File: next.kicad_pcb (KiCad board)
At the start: 2 copper layers, 351.4 x 99.7 mm, 193 parts, among them J1 USB_mini_micro_B, K0:0 KEYSW, K0:1 KEYSW, K0:2 KEYSW, K0:3 KEYSW, K0:3_1 KEYSW, K0:4 KEYSW, K0:4_1 KEYSW, K10:0 KEYSW, K10:1 KEYSW, K10:2 KEYSW, K10:3 KEYSW, K11:0 KEYSW, K11:1 KEYSW, K11:2 KEYSW, K11:3 KEYSW, K12:0 KEYSW, K12:1 KEYSW, K12:2 KEYSW, K12:3 KEYSW, K13:0 KEYSW, K13:1 KEYSW, K13:2 KEYSW, K13:3 KEYSW, K14:0 KEYSW, K14:1 KEYSW, K14:2 KEYSW, K14:3 KEYSW, K14:4 KEYSW, K14:4_1 KEYSW, K15:0 KEYSW, K15:1 KEYSW, K15:2 KEYSW, K15:3 KEYSW, K15:4 KEYSW, K16:0 KEYSW, K16:1 KEYSW, K16:2 KEYSW, K16:3 KEYSW, K16:4 KEYSW, K1:0 KEYSW, K1:1 KEYSW, K1:2 KEYSW, K1:3 KEYSW, K1:4 KEYSW, K1:4_1 KEYSW, K2:0 KEYSW, K2:1 KEYSW, K2:2 KEYSW, K2:3 KEYSW, K2:4 KEYSW, K2:4_1 KEYSW, K3:0 KEYSW, K3:1 KEYSW, K3:2 KEYSW, K3:3 KEYSW, K3:3_1 KEYSW, K3:4 KEYSW, K4:0 KEYSW, K4:1 KEYSW, K4:2 KEYSW, K4:3 KEYSW, K4:4 KEYSW, K5:0 KEYSW, K5:1 KEYSW, K5:2 KEYSW, K5:3 KEYSW, K5:4 KEYSW, K5:4_1 KEYSW, K6:0 KEYSW, K6:1 KEYSW, K6:2 KEYSW, K6:3 KEYSW, K7:0 KEYSW, K7:1 KEYSW, K7:2 KEYSW, K7:3 KEYSW, K8:0 KEYSW, K8:1 KEYSW, K8:2 KEYSW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

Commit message: V2
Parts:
- removed 7u_Stab: , Keyboard_Footprints:7u_stab
- removed C10: 1uF, Capacitors_SMD:C_0805
- removed the C3 at (200.0, 120.5)
- removed C9: 4.7uF, Capacitors_SMD:C_1206
- removed the D0:4 at (47.6, 104.8)
- removed D10:0, D7:1: D, Keyboard_Footprints:Diode_123
- removed D10:3, D5:4, D7:3, D8:0, D8:1, D8:2, D8:3, D9:0, D9:1, D9:2, D9:3, D9:4: D, Keyboard_Footprints:D_SOD123_axial
- removed K0:4_1, K14:4_1, K16:1, K16:2, K16:3, K16:4, K1:4_1, K2:4_1, K5:4_1: KEYSW, Keyboard_Footprints:Alps_SKCM
- removed the K1:0 at (57.1, 38.1)
- removed the K1:2 at (57.1, 76.2)
- removed the K1:3 at (57.1, 95.2)
- removed the K1:4 at (57.1, 114.3)
- removed LED4: LED, Keyboard_Footprints:LED_Rectangular_W3.9mm_H1.8mm_FlatTop
- removed SJ1, SJ2: SOLDER_JUMPER, Keyboard_Footprints:SOLDER_JUMPER_2
- removed Via (x2): Via, Keyboard_Footprints:Via
- added C8: 0.1uF, Capacitor_SMD:C_0805_2012Metric, B.Cu at (216.5, 107.8)
- added D0:10: D, Diode_SMD:D_SOD-123, B.Cu at (233.4, 40.5)
- added D0:8: D, Keyboard_Footprints:Diode_123_Axial, B.Cu at (181.0, 40.5)
- added D0:9: D, Keyboard_Footprints:Diode_123_Axial, B.Cu at (219.1, 40.5)
- added D1:7: D, Diode_SMD:D_SOD-123, B.Cu at (185.7, 59.5)
- added D1:8: D, Keyboard_Footprints:Diode_123_Axial, B.Cu at (190.5, 59.5)
- added D1:9: D, Keyboard_Footprints:Diode_123_Axial, B.Cu at (228.6, 59.5)
- added D2:8: D, Keyboard_Footprints:Diode_123_Axial, B.Cu at (195.3, 78.6)
- added D2:9: D, Keyboard_Footprints:Diode_123_Axial, B.Cu at (233.4, 78.6)
- added D3:10: D, Diode_SMD:D_SOD-123, B.Cu at (257.2, 97.6)
- added D3:7: D, Diode_SMD:D_SOD-123, B.Cu at (190.5, 97.6)
- added D3:8: D, Keyboard_Footprints:Diode_123_Axial, B.Cu at (204.8, 92.9)
- added D3:9: D, Keyboard_Footprints:Diode_123_Axial, B.Cu at (242.9, 92.9)
- added D4:0: D, Diode_SMD:D_SOD-123, B.Cu at (42.9, 116.7)
- added D4:5: D, Diode_SMD:D_SOD-123, B.Cu at (152.4, 116.7)
- added D4:9: D, Diode_SMD:D_SOD-123, B.Cu at (247.7, 116.7)
- added K0:1: KEYSW, Keyboard_Footprints:Alps, F.Cu at (57.1, 38.1)
- added K1:16: KEYSW, Keyboard_Footprints:Alps, F.Cu at (371.5, 57.1)
- added K2:1: KEYSW, Keyboard_Footprints:Alps, F.Cu at (57.1, 76.2)
- added K2:16: KEYSW, Keyboard_Footprints:Alps, F.Cu at (364.3, 76.2)
- added K3:1: KEYSW, Keyboard_Footprints:Alps, F.Cu at (57.1, 95.2)
- added K3:16: KEYSW, Keyboard_Footprints:Alps, F.Cu at (359.6, 95.2)
- added K4:0_1: KEYSW, Keyboard_Footprints:Alps_Secondary, F.Cu at (47.6, 114.3)
- added K4:1: KEYSW, Keyboard_Footprints:Alps, F.Cu at (57.1, 114.3)
- added K4:16: KEYSW, Keyboard_Footprints:Alps, F.Cu at (366.5, 114.3)
- added K4:1_1: KEYSW, Keyboard_Footprints:Alps_Secondary, F.Cu at (66.7, 114.3)
- added K4:2_1: KEYSW, Keyboard_Footprints:Alps_Secondary, F.Cu at (85.7, 114.3)
- C1, C2, C5, C6, C7: footprint Capacitors_SMD:C_0805 -> Capacitor_SMD:C_0805_2012Metric
- C3: renamed from C8; footprint Capacitors_SMD:C_0805 -> Capacitor_SMD:C_0805_2012Metric
- C4: value 0.1uF -> 4.7uF; footprint Capacitors_SMD:C_0805 -> Capacitor_SMD:C_0805_2012Metric
- D0:0, D1:1, D2:2, D3:3, D4:4: footprint Keyboard_Footprints:Diode_123 -> Diode_SMD:D_SOD-123; moved to B.Cu
- D0:1: renamed from D1:0; footprint Keyboard_Footprints:Diode_123 -> Diode_SMD:D_SOD-123; moved to B.Cu
- D0:11: renamed from D11:0; footprint Keyboard_Footprints:Diode_123 -> Diode_SMD:D_SOD-123; moved to B.Cu
- D0:12: renamed from D12:0; footprint Keyboard_Footprints:Diode_123 -> Diode_SMD:D_SOD-123; moved to B.Cu
- D0:13: renamed from D13:0; footprint Keyboard_Footprints:Diode_123 -> Diode_SMD:D_SOD-123; moved to B.Cu
- D0:14: renamed from D14:0; footprint Keyboard_Footprints:Diode_123 -> Diode_SMD:D_SOD-123; moved to B.Cu
- D0:15: renamed from D15:0; footprint Keyboard_Footprints:Diode_123 -> Diode_SMD:D_SOD-123; moved to B.Cu
- D0:16: renamed from D16:0; footprint Keyboard_Footprints:Diode_123 -> Diode_SMD:D_SOD-123; moved to B.Cu
- D0:2: renamed from D2:0; footprint Keyboard_Footprints:Diode_123 -> Diode_SMD:D_SOD-123; moved to B.Cu
- D0:3: renamed from D3:0; footprint Keyboard_Footprints:Diode_123 -> Diode_SMD:D_SOD-123; moved to B.Cu
- D0:4: renamed from D4:0; footprint Keyboard_Footprints:Diode_123 -> Diode_SMD:D_SOD-123; moved to B.Cu
- D0:5: renamed from D5:0; footprint Keyboard_Footprints:Diode_123 -> Diode_SMD:D_SOD-123; moved to B.Cu
- D0:6: renamed from D6:0; footprint Keyboard_Footprints:Diode_123 -> Diode_SMD:D_SOD-123; moved to B.Cu
- D0:7: renamed from D7:0; footprint Keyboard_Footprints:Diode_123 -> Diode_SMD:D_SOD-123; moved to B.Cu
- D1:0: renamed from D0:1; footprint Keyboard_Footprints:Diode_123 -> Diode_SMD:D_SOD-123; moved to B.Cu
- D1:10: renamed from D10:1; footprint Keyboard_Footprints:Diode_123 -> Diode_SMD:D_SOD-123; moved to B.Cu
- D1:11: renamed from D11:1; footprint Keyboard_Footprints:Diode_123 -> Diode_SMD:D_SOD-123; moved to B.Cu
- D1:12: renamed from D12:1; footprint Keyboard_Footprints:Diode_123 -> Diode_SMD:D_SOD-123; moved to B.Cu
- D1:13: renamed from D13:1; footprint Keyboard_Footprints:Diode_123 -> Diode_SMD:D_SOD-123; moved to B.Cu
- D1:14: renamed from D14:1; footprint Keyboard_Footprints:Diode_123 -> Diode_SMD:D_SOD-123; moved to B.Cu
- D1:15: renamed from D15:1; footprint Keyboard_Footprints:Diode_123 -> Diode_SMD:D_SOD-123; moved to B.Cu
- D1:16: renamed from D16:1; footprint Keyboard_Footprints:Diode_123 -> Diode_SMD:D_SOD-123; moved to B.Cu
- D1:2: renamed from D2:1; footprint Keyboard_Footprints:Diode_123 -> Diode_SMD:D_SOD-123; moved to B.Cu
- D1:3: renamed from D3:1; footprint Keyboard_Footprints:Diode_123 -> Diode_SMD:D_SOD-123; moved to B.Cu
- D1:4: renamed from D4:1; footprint Keyboard_Footprints:Diode_123 -> Diode_SMD:D_SOD-123; moved to B.Cu
- D1:5: renamed from D5:1; footprint Keyboard_Footprints:Diode_123 -> Diode_SMD:D_SOD-123; moved to B.Cu
- D1:6: renamed from D6:1; footprint Keyboard_Footprints:Diode_123 -> Diode_SMD:D_SOD-123; moved to B.Cu
- D2:0: renamed from D0:2; footprint Keyboard_Footprints:Diode_123 -> Diode_SMD:D_SOD-123; moved to B.Cu
- D2:1: renamed from D1:2; footprint Keyboard_Footprints:Diode_123 -> Diode_SMD:D_SOD-123; moved to B.Cu
- D2:10: renamed from D10:2; footprint Keyboard_Footprints:Diode_123 -> Diode_SMD:D_SOD-123; moved to B.Cu
- D2:11: renamed from D11:2; footprint Keyboard_Footprints:Diode_123 -> Diode_SMD:D_SOD-123; moved to B.Cu
- D2:12: renamed from D12:2; footprint Keyboard_Footprints:Diode_123 -> Diode_SMD:D_SOD-123; moved to B.Cu
- D2:13: renamed from D13:2; footprint Keyboard_Footprints:Diode_123 -> Diode_SMD:D_SOD-123; moved to B.Cu
- D2:14: renamed from D14:2; footprint Keyboard_Footprints:Diode_123 -> Diode_SMD:D_SOD-123; moved to B.Cu
- D2:15: renamed from D15:2; footprint Keyboard_Footprints:Diode_123 -> Diode_SMD:D_SOD-123; moved to B.Cu
- D2:16: renamed from D16:2; footprint Keyboard_Footprints:Diode_123 -> Diode_SMD:D_SOD-123; moved to B.Cu
- D2:3: renamed from D3:2; footprint Keyboard_Footprints:Diode_123 -> Diode_SMD:D_SOD-123; moved to B.Cu
- D2:4: renamed from D4:2; footprint Keyboard_Footprints:Diode_123 -> Diode_SMD:D_SOD-123; moved to B.Cu
- D2:5: renamed from D5:2; footprint Keyboard_Footprints:Diode_123 -> Diode_SMD:D_SOD-123; moved to B.Cu
- D2:6: renamed from D6:2; footprint Keyboard_Footprints:Diode_123 -> Diode_SMD:D_SOD-123; moved to B.Cu
- D2:7: renamed from D7:2; footprint Keyboard_Footprints:Diode_123 -> Diode_SMD:D_SOD-123; moved to B.Cu
- D3:0: renamed from D0:3; footprint Keyboard_Footprints:Diode_123 -> Diode_SMD:D_SOD-123; moved to B.Cu
- D3:1: renamed from D1:3; footprint Keyboard_Footprints:Diode_123 -> Diode_SMD:D_SOD-123; moved to B.Cu
- D3:11: renamed from D11:3; footprint Keyboard_Footprints:Diode_123 -> Diode_SMD:D_SOD-123; moved to B.Cu
- D3:12: renamed from D12:3; footprint Keyboard_Footprints:Diode_123 -> Diode_SMD:D_SOD-123; moved to B.Cu
- D3:13: renamed from D13:3; footprint Keyboard_Footprints:Diode_123 -> Diode_SMD:D_SOD-123; moved to B.Cu
- D3:14: renamed from D14:3; footprint Keyboard_Footprints:Diode_123 -> Diode_SMD:D_SOD-123; moved to B.Cu
- D3:15: renamed from D15:3; footprint Keyboard_Footprints:Diode_123 -> Diode_SMD:D_SOD-123; moved to B.Cu
- D3:16: renamed from D16:3; footprint Keyboard_Footprints:Diode_123 -> Diode_SMD:D_SOD-123; moved to B.Cu
- D3:2: renamed from D2:3; footprint Keyboard_Footprints:Diode_123 -> Diode_SMD:D_SOD-123; moved to B.Cu
- D3:4: renamed from D4:3; footprint Keyboard_Footprints:Diode_123 -> Diode_SMD:D_SOD-123; moved to B.Cu
- D3:5: renamed from D5:3; footprint Keyboard_Footprints:Diode_123 -> Diode_SMD:D_SOD-123; moved to B.Cu
- D3:6: renamed from D6:3; footprint Keyboard_Footprints:Diode_123 -> Diode_SMD:D_SOD-123; moved to B.Cu
- D4:1: renamed from D1:4; footprint Keyboard_Footprints:Diode_123 -> Diode_SMD:D_SOD-123; moved to B.Cu
- D4:14: renamed from D14:4; footprint Keyboard_Footprints:Diode_123 -> Diode_SMD:D_SOD-123; moved to B.Cu
- D4:15: renamed from D15:4; footprint Keyboard_Footprints:Diode_123 -> Diode_SMD:D_SOD-123; moved to B.Cu
- D4:16: renamed from D16:4; footprint Keyboard_Footprints:Diode_123 -> Diode_SMD:D_SOD-123; moved to B.Cu
- D4:2: renamed from D2:4; footprint Keyboard_Footprints:Diode_123 -> Diode_SMD:D_SOD-123; moved to B.Cu
- D4:3: renamed from D3:4; footprint Keyboard_Footprints:Diode_123 -> Diode_SMD:D_SOD-123; moved to B.Cu
- K0:0, K1:1, K2:2, K3:3, K4:4: footprint Keyboard_Footprints:Alps_SKCM -> Keyboard_Footprints:Alps
- K0:10: renamed from K10:0; footprint Keyboard_Footprints:Alps_SKCM -> Keyboard_Footprints:Alps
- K0:11: renamed from K11:0; footprint Keyboard_Footprints:Alps_SKCM -> Keyboard_Footprints:Alps
- K0:12: renamed from K12:0; footprint Keyboard_Footprints:Alps_SKCM -> Keyboard_Footprints:Alps
- K0:13: renamed from K13:0; footprint Keyboard_Footprints:Alps_SKCM -> Keyboard_Footprints:Alps
- K0:14: renamed from K14:0; footprint Keyboard_Footprints:Alps_SKCM -> Keyboard_Footprints:Alps
- K0:15: renamed from K15:0; footprint Keyboard_Footprints:Alps_SKCM -> Keyboard_Footprints:Alps
- K0:16: renamed from K16:0; footprint Keyboard_Footprints:Alps_SKCM -> Keyboard_Footprints:Alps
- K0:2: renamed from K2:0; footprint Keyboard_Footprints:Alps_SKCM -> Keyboard_Footprints:Alps
- K0:3: renamed from K3:0; footprint Keyboard_Footprints:Alps_SKCM -> Keyboard_Footprints:Alps
- K0:3_1, K3:3_1: footprint Keyboard_Footprints:Alps_SKCM -> Keyboard_Footprints:Alps_Secondary
- K0:4: renamed from K4:0; footprint Keyboard_Footprints:Alps_SKCM -> Keyboard_Footprints:Alps
- K0:5: renamed from K5:0; footprint Keyboard_Footprints:Alps_SKCM -> Keyboard_Footprints:Alps
- K0:6: renamed from K6:0; footprint Keyboard_Footprints:Alps_SKCM -> Keyboard_Footprints:Alps
- K0:7: renamed from K7:0; footprint Keyboard_Footprints:Alps_SKCM -> Keyboard_Footprints:Alps
- K0:8: renamed from K8:0; footprint Keyboard_Footprints:Alps_SKCM -> Keyboard_Footprints:Alps
- K0:9: renamed from K9:0; footprint Keyboard_Footprints:Alps_SKCM -> Keyboard_Footprints:Alps
- K1:0: renamed from K0:1; footprint Keyboard_Footprints:Alps_SKCM -> Keyboard_Footprints:Alps
- K1:10: renamed from K10:1; footprint Keyboard_Footprints:Alps_SKCM -> Keyboard_Footprints:Alps
- K1:11: renamed from K11:1; footprint Keyboard_Footprints:Alps_SKCM -> Keyboard_Footprints:Alps
- K1:12: renamed from K12:1; footprint Keyboard_Footprints:Alps_SKCM -> Keyboard_Footprints:Alps
- K1:13: renamed from K13:1; footprint Keyboard_Footprints:Alps_SKCM -> Keyboard_Footprints:Alps
- K1:14: renamed from K14:1; footprint Keyboard_Footprints:Alps_SKCM -> Keyboard_Footprints:Alps
- K1:15: renamed from K15:1; footprint Keyboard_Footprints:Alps_SKCM -> Keyboard_Footprints:Alps
- K1:2: renamed from K2:1; footprint Keyboard_Footprints:Alps_SKCM -> Keyboard_Footprints:Alps
- K1:3: renamed from K3:1; footprint Keyboard_Footprints:Alps_SKCM -> Keyboard_Footprints:Alps
- K1:4: renamed from K4:1; footprint Keyboard_Footprints:Alps_SKCM -> Keyboard_Footprints:Alps
- K1:5: renamed from K5:1; footprint Keyboard_Footprints:Alps_SKCM -> Keyboard_Footprints:Alps
- K1:6: renamed from K6:1; footprint Keyboard_Footprints:Alps_SKCM -> Keyboard_Footprints:Alps
- K1:7: renamed from K7:1; footprint Keyboard_Footprints:Alps_SKCM -> Keyboard_Footprints:Alps
- K1:8: renamed from K8:1; footprint Keyboard_Footprints:Alps_SKCM -> Keyboard_Footprints:Alps
- K1:9: renamed from K9:1; footprint Keyboard_Footprints:Alps_SKCM -> Keyboard_Footprints:Alps
- K2:0: renamed from K0:2; footprint Keyboard_Footprints:Alps_SKCM -> Keyboard_Footprints:Alps
- K2:10: renamed from K10:2; footprint Keyboard_Footprints:Alps_SKCM -> Keyboard_Footprints:Alps
- K2:11: renamed from K11:2; footprint Keyboard_Footprints:Alps_SKCM -> Keyboard_Footprints:Alps
- K2:12: renamed from K12:2; footprint Keyboard_Footprints:Alps_SKCM -> Keyboard_Footprints:Alps
- K2:13: renamed from K13:2; footprint Keyboard_Footprints:Alps_SKCM -> Keyboard_Footprints:Alps
- K2:14: renamed from K14:2; footprint Keyboard_Footprints:Alps_SKCM -> Keyboard_Footprints:Alps
- K2:15: renamed from K15:2; footprint Keyboard_Footprints:Alps_SKCM -> Keyboard_Footprints:Alps
- K2:3: renamed from K3:2; footprint Keyboard_Footprints:Alps_SKCM -> Keyboard_Footprints:Alps
- K2:4: renamed from K4:2; footprint Keyboard_Footprints:Alps_SKCM -> Keyboard_Footprints:Alps
- K2:5: renamed from K5:2; footprint Keyboard_Footprints:Alps_SKCM -> Keyboard_Footprints:Alps
- K2:6: renamed from K6:2; footprint Keyboard_Footprints:Alps_SKCM -> Keyboard_Footprints:Alps
- K2:7: renamed from K7:2; footprint Keyboard_Footprints:Alps_SKCM -> Keyboard_Footprints:Alps
- K2:8: renamed from K8:2; footprint Keyboard_Footprints:Alps_SKCM -> Keyboard_Footprints:Alps
- K2:9: renamed from K9:2; footprint Keyboard_Footprints:Alps_SKCM -> Keyboard_Footprints:Alps
- K3:0: renamed from K0:3; footprint Keyboard_Footprints:Alps_SKCM -> Keyboard_Footprints:Alps
- K3:10: renamed from K10:3; footprint Keyboard_Footprints:Alps_SKCM -> Keyboard_Footprints:Alps
- K3:11: renamed from K11:3; footprint Keyboard_Footprints:Alps_SKCM -> Keyboard_Footprints:Alps
- K3:12: renamed from K12:3; footprint Keyboard_Footprints:Alps_SKCM -> Keyboard_Footprints:Alps
- K3:13: renamed from K13:3; footprint Keyboard_Footprints:Alps_SKCM -> Keyboard_Footprints:Alps
- K3:14: renamed from K14:3; footprint Keyboard_Footprints:Alps_SKCM -> Keyboard_Footprints:Alps
- K3:15: renamed from K15:3; footprint Keyboard_Footprints:Alps_SKCM -> Keyboard_Footprints:Alps
- K3:2: renamed from K2:3; footprint Keyboard_Footprints:Alps_SKCM -> Keyboard_Footprints:Alps
- K3:4: renamed from K4:3; footprint Keyboard_Footprints:Alps_SKCM -> Keyboard_Footprints:Alps
- K3:5: renamed from K5:3; footprint Keyboard_Footprints:Alps_SKCM -> Keyboard_Footprints:Alps
- K3:6: renamed from K6:3; footprint Keyboard_Footprints:Alps_SKCM -> Keyboard_Footprints:Alps
- K3:7: renamed from K7:3; footprint Keyboard_Footprints:Alps_SKCM -> Keyboard_Footprints:Alps
- K3:8: renamed from K8:3; footprint Keyboard_Footprints:Alps_SKCM -> Keyboard_Footprints:Alps
- K3:9: renamed from K9:3; footprint Keyboard_Footprints:Alps_SKCM -> Keyboard_Footprints:Alps
- K4:0: renamed from K0:4; footprint Keyboard_Footprints:Alps_SKCM -> Keyboard_Footprints:Alps
- K4:14: renamed from K14:4; footprint Keyboard_Footprints:Alps_SKCM -> Keyboard_Footprints:Alps
- K4:15: renamed from K15:4; footprint Keyboard_Footprints:Alps_SKCM -> Keyboard_Footprints:Alps
- K4:2: renamed from K2:4; footprint Keyboard_Footprints:Alps_SKCM -> Keyboard_Footprints:Alps
- K4:3: renamed from K3:4; footprint Keyboard_Footprints:Alps_SKCM -> Keyboard_Footprints:Alps
- K4:5: renamed from K5:4; footprint Keyboard_Footprints:Alps_SKCM -> Keyboard_Footprints:Alps
- K4:9: renamed from K9:4; footprint Keyboard_Footprints:Alps_SKCM -> Keyboard_Footprints:Alps
- LED1, LED2, LED3: footprint Keyboard_Footprints:LED_Rectangular_W3.9mm_H1.8mm_FlatTop -> LED_THT:LED_D3.0mm
- R1, R2, R3, R5, R6, R7: footprint Resistors_SMD:R_0805 -> Resistor_SMD:R_0805_2012Metric
- R4: value 1k -> 10k; footprint Resistors_SMD:R_0805 -> Resistor_SMD:R_0805_2012Metric
- SW1: value SW_JUMP -> RESET; footprint Pin_Headers:Pin_Header_Straight_1x02_Pitch1.27mm -> Keyboard_Footprints:TE_1825966-1; moved to B.Cu
- U1: footprint Keyboard_Footprints:ATmega32U4-AU -> Package_QFP:LQFP-44_10x10mm_P0.8mm
- X1: value XTAL_GND -> 16MHz_12pF; footprint Keyboard_Footprints:Crystal_SMD_3225-4pin_3.2x2.5mm -> Crystal:Crystal_SMD_SeikoEpson_FA238-4Pin_3.2x2.5mm
- moved R4 167.8 mm to (348.5, 115.2), turned to -90 degrees
- moved C7 26.5 mm to (193.0, 108.0), turned to 180 degrees
- moved C4 16.1 mm to (221.2, 111.2), turned to 90 degrees
- moved D4:1 12.8 mm to (61.9, 116.7), turned to 90 degrees
- moved C6 12.6 mm to (208.5, 101.0)
- moved D4:3 10.6 mm to (100.0, 116.7), turned to 90 degrees
- moved C5 10.6 mm to (199.2, 120.0), turned to 90 degrees
- moved D0:15 9.53 mm to (328.6, 40.5), turned to 90 degrees
- moved D0:16 9.53 mm to (371.5, 40.5), turned to 90 degrees
- moved D1:12 9.53 mm to (281.0, 59.5), turned to 90 degrees
- moved D1:13 9.53 mm to (300.0, 59.5), turned to 90 degrees
- moved D1:16 9.53 mm to (376.2, 59.5), turned to 90 degrees
- moved D2:13 9.53 mm to (304.8, 78.6), turned to 90 degrees
- moved D2:14 9.53 mm to (323.9, 78.6), turned to 90 degrees
- moved D3:11 9.53 mm to (276.2, 97.6), turned to 90 degrees
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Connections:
- net Net-(D0:0-Pad1) renamed Row0
- net Net-(D0:4-Pad1) renamed Row4
- net Net-(K0:0-Pad1) renamed Col0
- net Net-(K1:0-Pad1) renamed Col1
- net Net-(K2:0-Pad1) renamed Col2
- net Net-(K3:0-Pad1) renamed Col3
- C7 pad 1: Net-(C7-Pad1) -> +5V
- D1:0 pad 1: Net-(D0:1-Pad1) -> Row1
- D1:1 pad 1: Net-(D0:1-Pad1) -> Row1
- D1:10 pad 1: Net-(D0:1-Pad1) -> Row1
- D1:11 pad 1: Net-(D0:1-Pad1) -> Row1
- D1:12 pad 1: Net-(D0:1-Pad1) -> Row1
- D1:13 pad 1: Net-(D0:1-Pad1) -> Row1
- D1:14 pad 1: Net-(D0:1-Pad1) -> Row1
- D1:15 pad 1: Net-(D0:1-Pad1) -> Row1
- D1:16 pad 1: Net-(D0:1-Pad1) -> Row1
- D1:2 pad 1: Net-(D0:1-Pad1) -> Row1
- D1:3 pad 1: Net-(D0:1-Pad1) -> Row1
- D1:4 pad 1: Net-(D0:1-Pad1) -> Row1
- D1:5 pad 1: Net-(D0:1-Pad1) -> Row1
- D1:6 pad 1: Net-(D0:1-Pad1) -> Row1
- D2:0 pad 1: Net-(D0:2-Pad1) -> Row2
- D2:1 pad 1: Net-(D0:2-Pad1) -> Row2
- D2:10 pad 1: Net-(D0:2-Pad1) -> Row2
- D2:11 pad 1: Net-(D0:2-Pad1) -> Row2
- D2:12 pad 1: Net-(D0:2-Pad1) -> Row2
- D2:13 pad 1: Net-(D0:2-Pad1) -> Row2
- D2:14 pad 1: Net-(D0:2-Pad1) -> Row2
- D2:15 pad 1: Net-(D0:2-Pad1) -> Row2
- D2:16 pad 1: Net-(D0:2-Pad1) -> Row2
- D2:2 pad 1: Net-(D0:2-Pad1) -> Row2
- D2:3 pad 1: Net-(D0:2-Pad1) -> Row2
- D2:4 pad 1: Net-(D0:2-Pad1) -> Row2
- D2:5 pad 1: Net-(D0:2-Pad1) -> Row2
- D2:6 pad 1: Net-(D0:2-Pad1) -> Row2
- D2:7 pad 1: Net-(D0:2-Pad1) -> Row2
- D3:0 pad 1: Net-(D0:3-Pad1) -> Row3
- D3:1 pad 1: Net-(D0:3-Pad1) -> Row3
- D3:11 pad 1: Net-(D0:3-Pad1) -> Row3
- D3:12 pad 1: Net-(D0:3-Pad1) -> Row3
- D3:13 pad 1: Net-(D0:3-Pad1) -> Row3
- D3:14 pad 1: Net-(D0:3-Pad1) -> Row3
- D3:15 pad 1: Net-(D0:3-Pad1) -> Row3
- D3:16 pad 1: Net-(D0:3-Pad1) -> Row3
- D3:2 pad 1: Net-(D0:3-Pad1) -> Row3
- D3:3 pad 1: Net-(D0:3-Pad1) -> Row3
- D3:4 pad 1: Net-(D0:3-Pad1) -> Row3
- D3:5 pad 1: Net-(D0:3-Pad1) -> Row3
- D3:6 pad 1: Net-(D0:3-Pad1) -> Row3
- J1 pad 4: Net-(J1-Pad4) -> unconnected-(J1-Pad4)
- J1 pad 6: Net-(J1-Pad6) -> unconnected-(J1-Pad6)
- K0:10 pad 1: Net-(K10:0-Pad1) -> Col10
- K0:11 pad 1: Net-(K11:0-Pad1) -> Col11
- K0:12 pad 1: Net-(K12:0-Pad1) -> Col12
- K0:13 pad 1: Net-(K13:0-Pad1) -> Col13
- K0:14 pad 1: Net-(K14:0-Pad1) -> Col14
- K0:15 pad 1: Net-(K15:0-Pad1) -> Col15
- K0:16 pad 1: Net-(K16:0-Pad1) -> Col16
- K0:4 pad 1: Net-(K4:0-Pad1) -> Col4
- K0:5 pad 1: Net-(K5:0-Pad1) -> Col5
- K0:6 pad 1: Net-(K6:0-Pad1) -> Col6
- K0:7 pad 1: Net-(K7:0-Pad1) -> Col7
- K0:8 pad 1: Net-(K8:0-Pad1) -> Col8
- K0:9 pad 1: Net-(K9:0-Pad1) -> Col9
- K1:10 pad 1: Net-(K10:0-Pad1) -> Col10
- K1:11 pad 1: Net-(K11:0-Pad1) -> Col11
- K1:12 pad 1: Net-(K12:0-Pad1) -> Col12
- K1:13 pad 1: Net-(K13:0-Pad1) -> Col13
- K1:14 pad 1: Net-(K14:0-Pad1) -> Col14
- K1:15 pad 1: Net-(K15:0-Pad1) -> Col15
- K1:4 pad 1: Net-(K4:0-Pad1) -> Col4
- K1:5 pad 1: Net-(K5:0-Pad1) -> Col5
- K1:6 pad 1: Net-(K6:0-Pad1) -> Col6
- K1:7 pad 1: Net-(K7:0-Pad1) -> Col7
- K1:8 pad 1: Net-(K8:0-Pad1) -> Col8
- K1:9 pad 1: Net-(K9:0-Pad1) -> Col9
- K2:10 pad 1: Net-(K10:0-Pad1) -> Col10
- K2:11 pad 1: Net-(K11:0-Pad1) -> Col11
- K2:12 pad 1: Net-(K12:0-Pad1) -> Col12
- K2:13 pad 1: Net-(K13:0-Pad1) -> Col13
- K2:14 pad 1: Net-(K14:0-Pad1) -> Col14
- K2:15 pad 1: Net-(K15:0-Pad1) -> Col15
- K2:4 pad 1: Net-(K4:0-Pad1) -> Col4
- K2:5 pad 1: Net-(K5:0-Pad1) -> Col5
- K2:6 pad 1: Net-(K6:0-Pad1) -> Col6
- K2:7 pad 1: Net-(K7:0-Pad1) -> Col7
- K2:8 pad 1: Net-(K8:0-Pad1) -> Col8
- K2:9 pad 1: Net-(K9:0-Pad1) -> Col9
- K3:10 pad 1: Net-(K10:0-Pad1) -> Col10
- K3:11 pad 1: Net-(K11:0-Pad1) -> Col11
- K3:12 pad 1: Net-(K12:0-Pad1) -> Col12
- K3:13 pad 1: Net-(K13:0-Pad1) -> Col13
- K3:14 pad 1: Net-(K14:0-Pad1) -> Col14
- K3:15 pad 1: Net-(K15:0-Pad1) -> Col15
- K3:4 pad 1: Net-(K4:0-Pad1) -> Col4
- K3:5 pad 1: Net-(K5:0-Pad1) -> Col5
- K3:6 pad 1: Net-(K6:0-Pad1) -> Col6
- K3:7 pad 1: Net-(K7:0-Pad1) -> Col7
- K3:8 pad 1: Net-(K8:0-Pad1) -> Col8
- K3:9 pad 1: Net-(K9:0-Pad1) -> Col9
- K4:14 pad 1: Net-(K14:0-Pad1) -> Col14
- K4:15 pad 1: Net-(K15:0-Pad1) -> Col15
- K4:4 pad 1: Net-(K4:0-Pad1) -> Col4
- K4:5 pad 1: Net-(K5:0-Pad1) -> Col5
- K4:9 pad 1: Net-(K9:0-Pad1) -> Col9
- R4 pad 1: GND -> +5V
- R4 pad 2: Net-(LED4-Pad2) -> Net-(R4-Pad2)
- R5 pad 1: Net-(LED1-Pad2) -> Net-(LED1-Pad1)
- R6 pad 1: Net-(LED2-Pad2) -> Net-(LED2-Pad1)
- R7 pad 1: Net-(LED3-Pad2) -> Net-(LED3-Pad1)
- SW1 pad 2: Net-(SW1-Pad2) -> Net-(R4-Pad2)
- U1 pad 10: Net-(K16:0-Pad1) -> Col14
- U1 pad 11: Net-(D0:2-Pad1) -> Col15
- U1 pad 12: Net-(D0:1-Pad1) -> Net-(LED3-Pad2)
- U1 pad 13: Net-(SW1-Pad2) -> Net-(R4-Pad2)
- U1 pad 22: Net-(LED1-Pad1) -> Col4
- U1 pad 26: Net-(SJ1-Pad1) -> Col5
- U1 pad 27: Net-(LED3-Pad1) -> Col6
- U1 pad 28: Net-(K4:0-Pad1) -> Col16
- U1 pad 29: Net-(K5:0-Pad1) -> Net-(LED1-Pad2)
- U1 pad 30: Net-(K6:0-Pad1) -> Net-(LED2-Pad2)
- U1 pad 31: Net-(K7:0-Pad1) -> Col10
- U1 pad 32: Net-(D0:3-Pad1) -> Col11
- U1 pad 36: Net-(K8:0-Pad1) -> Row3
- U1 pad 37: Net-(K9:0-Pad1) -> Row2
- U1 pad 38: Net-(K10:0-Pad1) -> Row1
- U1 pad 39: Net-(K11:0-Pad1) -> Col9
- U1 pad 40: Net-(K12:0-Pad1) -> Col8
- U1 pad 41: Net-(K13:0-Pad1) -> Col7
- U1 pad 42: Net-(C7-Pad1) -> unconnected-(U1-Pad42)
- U1 pad 8: Net-(K14:0-Pad1) -> Col12
- U1 pad 9: Net-(K15:0-Pad1) -> Col13
- X1 pad 2: Net-(C2-Pad1) -> GND
- X1 pad 3: GND -> Net-(C2-Pad1)
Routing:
- net Net-(D0:1-Pad1): track 558.1 -> 0.00 mm, vias 2 -> 0
- net Net-(D0:2-Pad1): track 513.7 -> 0.00 mm, vias 2 -> 0
- net Net-(D0:3-Pad1): track 410.7 -> 0.00 mm
- net Row3: track 0.00 -> 397.9 mm, vias 0 -> 1
- net Row1: track 0.00 -> 388.5 mm
- net GND: track 128.6 -> 516.4 mm, vias 19 -> 7
- net Row2: track 0.00 -> 362.2 mm
- net Net-(K15:0-Pad1): track 274.5 -> 0.00 mm, vias 1 -> 0
- net Col16: track 0.00 -> 270.6 mm, vias 0 -> 2
- net Net-(K16:0-Pad1): track 262.8 -> 0.00 mm, vias 2 -> 0
- net Col15: track 0.00 -> 261.0 mm, vias 0 -> 1
- net Net-(K14:0-Pad1): track 250.8 -> 0.00 mm
- net Net-(LED3-Pad1): track 247.8 -> 4.30 mm, vias 4 -> 0
- net Col14: track 0.00 -> 230.5 mm, vias 0 -> 1
- net Net-(LED1-Pad2): track 2.54 -> 218.5 mm
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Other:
- net class D2 removed
- net class D3 removed
- net class D4 removed
- net class Default removed
- rule pad_to_mask_clearance: 0.2 -> 0
- board text added: "NeXT76 by Andrew D Rev 1.1"
- board text removed: "NeXT76 by Andrew D Rev 1.0"

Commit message: Update Model
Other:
- board text added: "NeXT76 by Andrew D Rev 1.0"
- board text removed: "NeXT76 by Andrew D Rev 1.1"
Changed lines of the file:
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@@
   (gr_arc (start 380.5 123) (mid 380.353553 123.353553) (end 380 123.5) (layer "Edge.Cuts") (width 0.1))
   (gr_line (start 29.6 29.1) (end 200.025 29.1) (layer "Edge.Cuts") (width 0.1))
-  (gr_text "NeXT76 by Andrew D\nRev 1.1\n" (at 290.5125 114.3) (layer "B.SilkS")
+  (gr_text "NeXT76 by Andrew D\nRev 1.0\n" (at 290.5125 114.3) (layer "B.SilkS")
     (effects (font (size 1.5 1.5) (thickness 0.3)) (justify mirror))
   )

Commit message: Update Axial_Diode Footprint
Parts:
- C1, C2: value 22pF -> 22p
- C3: value 1uF -> 1u
- C4: value 4.7uF -> 4.7u
- C5, C6, C7, C8: value 0.1uF -> 0.1u
- turned D0:8 to 90 degrees
- turned D0:9 to 90 degrees
- turned D1:8 to 90 degrees
- turned D1:9 to 90 degrees
- turned D2:8 to 90 degrees
- turned D2:9 to 90 degrees
- turned D3:8 to 90 degrees
- turned D3:9 to 90 degrees

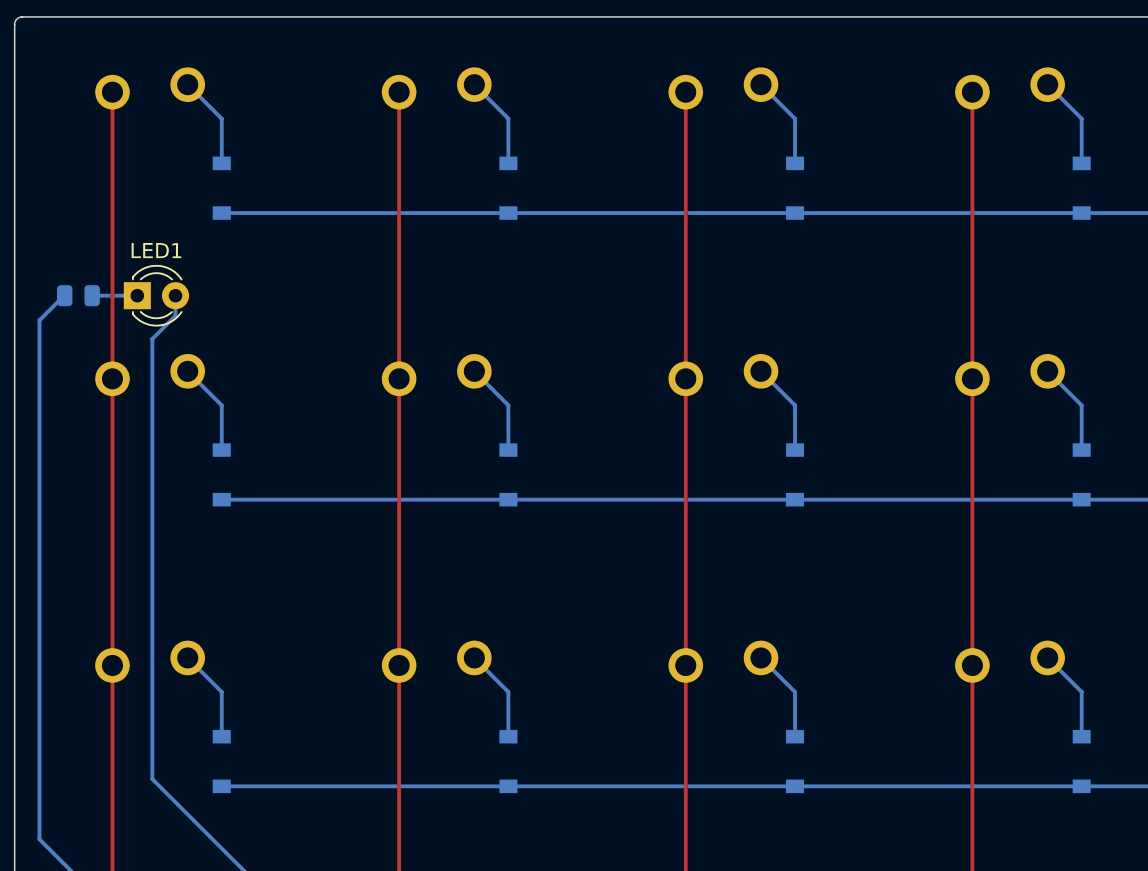
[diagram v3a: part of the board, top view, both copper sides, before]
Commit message: Added LED opttion
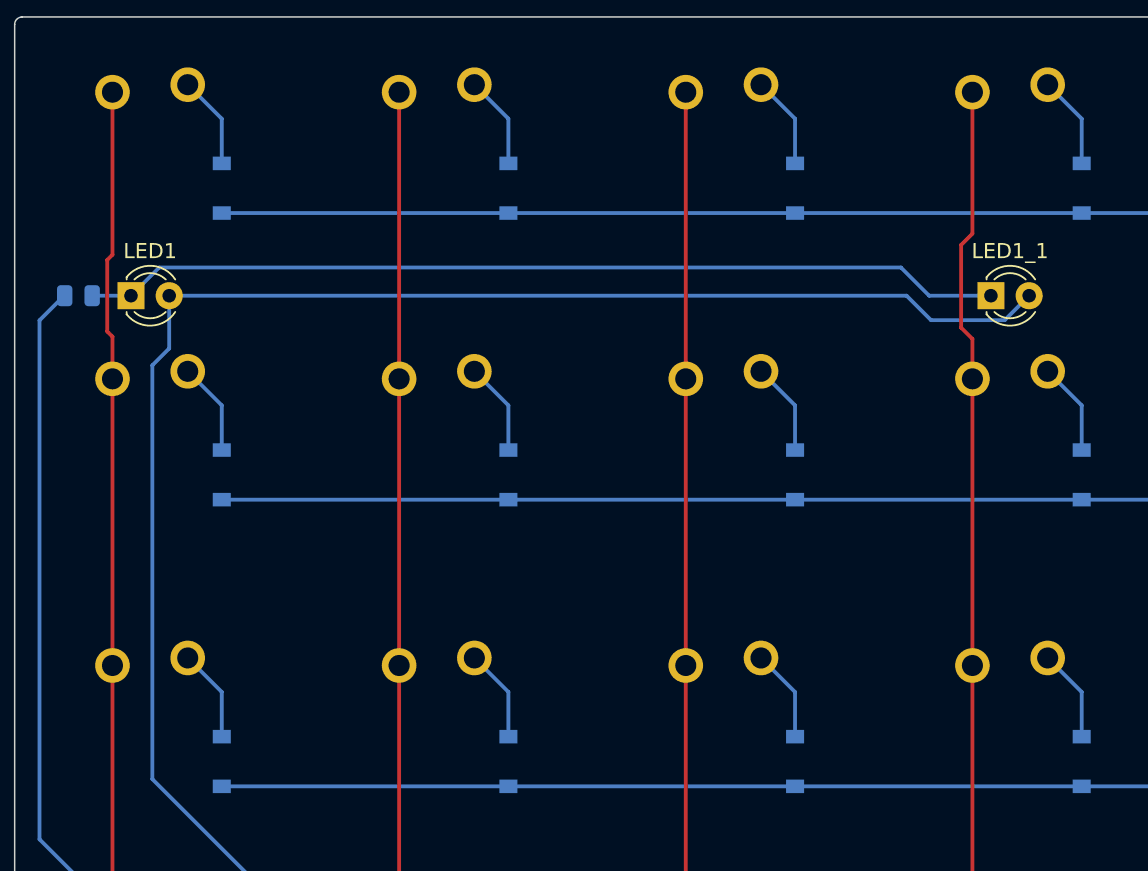
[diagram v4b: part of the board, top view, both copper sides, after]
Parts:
- added LED1_1: LED, LED_THT:LED_D3.0mm, F.Cu at (94.0, 47.6)
- moved LED1 0.42 mm to (36.8, 47.6)
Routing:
- net Net-(LED1-Pad2): track 218.5 -> 276.8 mm
- net Net-(LED1-Pad1): track 2.96 -> 61.3 mm
- net Col3: track 184.6 -> 185.2 mm
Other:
- board text added: "NeXT76 by Andrew D Rev 1.1"
- board text removed: "NeXT76 by Andrew D Rev 1.0"
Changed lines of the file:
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@@
   )
   (footprint "LED_THT:LED_D3.0mm" (layer "F.Cu")
-    (at 37.25 47.625)
+    (at 36.83 47.625)
     (descr "LED, diameter 3.0mm, 2 pins")
     (tags "LED diameter 3.0mm 2 pins")
@@
       (net 27 "Net-(D4:1-Pad2)") (pintype "passive"))
   )
+  (footprint "LED_THT:LED_D3.0mm" (layer "F.Cu")
+    (at 93.98 47.625)
+    (descr "LED, diameter 3.0mm, 2 pins")
+    (tags "LED diameter 3.0mm 2 pins")
+    (property "Sheetfile" "next.kicad_sch")
+    (property "Sheetname" "")
+    (attr through_hole)
+    (fp_text reference "LED1_1" (at 1.27 -2.96) (layer "F.SilkS")
+      (effects (font (size 1 1) (thickness 0.15)))
+    )
+    (fp_text value "LED" (at 1.27 2.96) (layer "F.Fab")
+      (effects (font (size 1 1) (thickness 0.15)))
+    )
+    (fp_line (start -0.29 1.08) (end -0.29 1.236) (layer "F.SilkS") (width 0.12))
+    (fp_line (start -0.29 -1.236) (end -0.29 -1.08) (layer "F.SilkS") (width 0.12))
+    (fp_arc (start 2.942335 1.078608) (mid 1.366487 1.987659) (end -0.29 1.235516) (layer "F.SilkS") (width 0.12))
+    (fp_arc (start 2.31113 1.079837) (mid 1.270117 1.5) (end 0.229039 1.08) (layer "F.SilkS") (width 0.12))
+    (fp_arc (start -0.29 -1.235516) (mid 1.366487 -1.987659) (end 2.942335 -1.078608) (layer "F.SilkS") (width 0.12))
+    (fp_arc (start 0.229039 -1.08) (mid 1.270117 -1.5) (end 2.31113 -1.079837) (layer "F.SilkS") (width 0.12))
+    (fp_line (start -1.15 2.25) (end 3.7 2.25) (layer "F.CrtYd") (width 0.05))
+    (fp_line (start -1.15 -2.25) (end -1.15 2.25) (layer "F.CrtYd") (width 0.05))
+    (fp_line (start 3.7 2.25) (end 3.7 -2.25) (layer "F.CrtYd") (width 0.05))
+    (fp_line (start 3.7 -2.25) (end -1.15 -2.25) (layer "F.CrtYd") (width 0.05))
+    (fp_line (start -0.23 -1.16619) (end -0.23 1.16619) (layer "F.Fab") (width 0.1))
+    (fp_arc (start -0.23 -1.16619) (mid 3.17 0.000452) (end -0.230555 1.165476) (layer "F.Fab") (width 0.1))
+    (fp_circle (center 1.27 0) (end 2.77 0) (layer "F.Fab") (width 0.1) (fill none))
+    (pad "1" thru_hole rect locked (at 0 0) (size 1.8 1.8) (drill 0.9) (layers *.Cu *.Mask)
+      (net 85 "Net-(LED1-Pad1)") (pinfunction "K") (pintype "passive"))
+    (pad "2" thru_hole circle locked (at 2.54 0) (size 1.8 1.8) (drill 0.9) (layers *.Cu *.Mask)
+      (net 86 "Net-(LED1-Pad2)") (pinfunction "A") (pintype "passive"))
+    (model "${KICAD6_3DMODEL_DIR}/LED_THT.3dshapes/LED_D3.0mm.wrl"
+      (offset (xyz 0 0 0))
+      (scale (xyz 1 1 1))
+      (rotate (xyz 0 0 0))
+    )
+  )
   (footprint "Diode_SMD:D_SOD-123" (layer "B.Cu")
     (at 42.8625 40.48125 90)
@@
       (effects (font (size 1 1) (thickness 0.15)) (justify mirror))
     )
+    (fp_line (start 3 -1.75) (end -3 -1.75) (layer "Cmts.User") (width 0.1))
     (fp_line (start -3 -1.75) (end -3 1.75) (layer "Cmts.User") (width 0.1))
     (fp_line (start -3 1.75) (end 3 1.75) (layer "Cmts.User") (width 0.1))
     (fp_line (start 3 1.75) (end 3 -1.75) (layer "Cmts.User") (width 0.1))
-    (fp_line (start 3 -1.75) (end -3 -1.75) (layer "Cmts.User") (width 0.1))
     (pad "1" thru_hole circle locked (at -3.25 0 270) (size 2 2) (drill 1.24) (layers *.Cu *.Mask)
       (net 2 "GND") (pinfunction "1") (pintype "passive"))
@@
   (gr_arc (start 380.5 123) (mid 380.353553 123.353553) (end 380 123.5) (layer "Edge.Cuts") (width 0.1))
   (gr_line (start 29.6 29.1) (end 200.025 29.1) (layer "Edge.Cuts") (width 0.1))
-  (gr_text "NeXT76 by Andrew D\nRev 1.0\n" (at 290.5125 114.3) (layer "B.SilkS")
+  (gr_text "NeXT76 by Andrew D\nRev 1.1\n" (at 290.5125 114.3) (layer "B.SilkS")
     (effects (font (size 1.5 1.5) (thickness 0.3)) (justify mirror))
   )
@@
   (segment (start 173.25 116.25) (end 171.16875 118.33125) (width 0.254) (layer "B.Cu") (net 84))
   (segment (start 333.375 118.33125) (end 247.65 118.33125) (width 0.254) (layer "B.Cu") (net 84))
-  (segment (start 34.2875 47.625) (end 37.25 47.625) (width 0.254) (layer "B.Cu") (net 85))
-  (segment (start 201.679111 106.54774) (end 198.25 103.118629) (width 0.254) (layer "B.Cu") (net 86))
-  (segment (start 198 86.25) (end 44.75 86.25) (width 0.254) (layer "B.Cu") (net 86))
-  (segment (start 38.25 50.5) (end 39.79 48.96) (width 0.254) (layer "B.Cu") (net 86))
-  (segment (start 44.75 86.25) (end 38.25 79.75) (width 0.254) (layer "B.Cu") (net 86))
-  (segment (start 200 88.25) (end 198 86.25) (width 0.254) (layer "B.Cu") (net 86))
+  (segment (start 89.875 47.625) (end 93.98 47.625) (width 0.25) (layer "B.Cu") (net 85))
+  (segment (start 38.705 45.75) (end 88 45.75) (width 0.25) (layer "B.Cu") (net 85))
+  (segment (start 36.83 47.625) (end 38.705 45.75) (width 0.25) (layer "B.Cu") (net 85))
+  (segment (start 88 45.75) (end 89.875 47.625) (width 0.25) (layer "B.Cu") (net 85))
+  (segment (start 34.25 47.625) (end 36.83 47.625) (width 0.25) (layer "B.Cu") (net 85))
   (segment (start 200 93.75) (end 200 88.25) (width 0.254) (layer "B.Cu") (net 86))
+  (segment (start 38.25 52.25) (end 39.37 51.13) (width 0.254) (layer "B.Cu") (net 86))
+  (segment (start 38.25 79.75) (end 38.25 52.25) (width 0.254) (layer "B.Cu") (net 86))
+  (segment (start 200 88.25) (end 198 86.25) (width 0.254) (layer "B.Cu") (net 86))
   (segment (start 198.25 103.118629) (end 198.25 95.5) (width 0.254) (layer "B.Cu") (net 86))
-  (segment (start 38.25 79.75) (end 38.25 50.5) (width 0.254) (layer "B.Cu") (net 86))
+  (segment (start 39.37 51.13) (end 39.37 47.625) (width 0.254) (layer "B.Cu") (net 86))
+  (segment (start 198 86.25) (end 44.75 86.25) (width 0.254) (layer "B.Cu") (net 86))
+  (segment (start 201.679111 106.54774) (end 198.25 103.118629) (width 0.254) (layer "B.Cu") (net 86))
+  (segment (start 94.895 49.25) (end 96.52 47.625) (width 0.254) (layer "B.Cu") (net 86))
+  (segment (start 44.75 86.25) (end 38.25 79.75) (width 0.254) (layer "B.Cu") (net 86))
+  (segment (start 88.375 47.625) (end 90 49.25) (width 0.254) (layer "B.Cu") (net 86))
+  (segment (start 90 49.25) (end 94.895 49.25) (width 0.254) (layer "B.Cu") (net 86))
   (segment (start 198.25 95.5) (end 200 93.75) (width 0.254) (layer "B.Cu") (net 86))
-  (segment (start 39.79 48.96) (end 39.79 47.625) (width 0.254) (layer "B.Cu") (net 86))
+  (segment (start 39.37 47.625) (end 88.375 47.625) (width 0.254) (layer "B.Cu") (net 86))
   (segment (start 143.2 91) (end 144.5 89.7) (width 0.254) (layer "B.Cu") (net 87))
   (segment (start 139.75 91) (end 143.2 91) (width 0.254) (layer "B.Cu") (net 87))
@@
   (segment (start 347.6625 35.8625) (end 345.4 33.6) (width 0.254) (layer "B.Cu") (net 95))
   (segment (start 347.6625 38.83125) (end 347.6625 35.8625) (width 0.254) (layer "B.Cu") (net 95))
-  (segment (start 35.6 72.2) (end 35.6 34.1) (width 0.254) (layer "F.Cu") (net 98))
+  (segment (start 35.25 45.25) (end 35.6 44.9) (width 0.254) (layer "F.Cu") (net 98))
+  (segment (start 35.6 44.9) (end 35.6 34.1) (width 0.254) (layer "F.Cu") (net 98))
+  (segment (start 35.6 50.35) (end 35.25 50) (width 0.254) (layer "F.Cu") (net 98))
   (segment (start 35.6 72.2) (end 35.6 91.25) (width 0.254) (layer "F.Cu") (net 98))
+  (segment (start 35.6 72.2) (end 35.6 53.15) (width 0.254) (layer "F.Cu") (net 98))
   (segment (start 35.6 105.775) (end 35.6 91.25) (width 0.254) (layer "F.Cu") (net 98))
+  (segment (start 35.6 53.15) (end 35.6 50.35) (width 0.254) (layer "F.Cu") (net 98))
   (segment (start 34.1 107.275) (end 35.6 105.775) (width 0.254) (layer "F.Cu") (net 98))
+  (segment (start 35.25 50) (end 35.25 45.25) (width 0.254) (layer "F.Cu") (net 98))
   (segment (start 34.1 108.8) (end 34.1 107.275) (width 0.254) (layer "B.Cu") (net 98))
   (segment (start 172.75 115.5) (end 171 117.25) (width 0.254) (layer "B.Cu") (net 98))
@@
   (segment (start 345.25 117.25) (end 346.3 116.2) (width 0.254) (layer "B.Cu") (net 101))
   (segment (start 245.25 117.25) (end 345.25 117.25) (width 0.254) (layer "B.Cu") (net 101))
+  (segment (start 92 49.75) (end 92 44.25) (width 0.254) (layer "F.Cu") (net 102))
   (segment (start 92.75 95.775) (end 99.25 102.275) (width 0.254) (layer "F.Cu") (net 102))
+  (segment (start 92.75 53.15) (end 92.75 50.5) (width 0.254) (layer "F.Cu") (net 102))
   (segment (start 92.75 91.25) (end 92.75 95.775) (width 0.254) (layer "F.Cu") (net 102))
+  (segment (start 92.75 72.2) (end 92.75 53.15) (width 0.254) (layer "F.Cu") (net 102))
+  (segment (start 92.75 43.5) (end 92.75 34.1) (width 0.254) (layer "F.Cu") (net 102))
   (segment (start 99.25 102.275) (end 92.75 108.775) (width 0.254) (layer "F.Cu") (net 102))
   (segment (start 92.75 72.2) (end 92.75 91.25) (width 0.254) (layer "F.Cu") (net 102))
-  (segment (start 92.75 72.2) (end 92.75 34.1) (width 0.254) (layer "F.Cu") (net 102))
+  (segment (start 92.75 50.5) (end 92 49.75) (width 0.254) (layer "F.Cu") (net 102))
   (segment (start 92.75 108.775) (end 92.75 110.3) (width 0.254) (layer "F.Cu") (net 102))
+  (segment (start 92 44.25) (end 92.75 43.5) (width 0.254) (layer "F.Cu") (net 102))
   (segment (start 199.522435 108.916548) (end 194.855887 104.25) (width 0.254) (layer "B.Cu") (net 102))
   (segment (start 194.855887 104.25) (end 101.225 104.25) (width 0.254) (layer "B.Cu") (net 102))

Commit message: Update diodes
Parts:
- D0:8, D0:9, D1:8, D1:9, D2:8, D2:9, D3:8, D3:9: footprint Keyboard_Footprints:Diode_123_Axial -> Diode_SMD:D_SOD-123
- moved D0:8 14.3 mm to (195.3, 40.5)
- moved D1:8 14.3 mm to (204.8, 59.5)
- moved D3:9 6.74 mm to (238.1, 97.6)
- moved D2:9 4.76 mm to (228.6, 78.6)
- moved D0:9 4.76 mm to (214.3, 40.5)
- moved D1:9 4.76 mm to (223.8, 59.5)
- moved D3:8 2.38 mm to (204.8, 95.2)
- moved R3 0.25 mm to (202.8, 101.0)
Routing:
- net Row0: track 432.0 -> 416.7 mm, vias 1 -> 2
- net Net-(D1:8-Pad2): track 14.4 -> 6.17 mm
- net Net-(D0:8-Pad2): track 13.3 -> 6.17 mm
- net Row2: track 362.2 -> 357.9 mm, vias 0 -> 2
- net Net-(D3:8-Pad2): track 12.8 -> 16.4 mm, vias 0 -> 1
- net Net-(D2:8-Pad2): track 13.3 -> 16.1 mm, vias 0 -> 1
- net Net-(D2:9-Pad2): track 8.26 -> 6.17 mm
- net Net-(D1:9-Pad2): track 8.26 -> 6.17 mm
- net Net-(D0:9-Pad2): track 8.26 -> 6.17 mm
- net Net-(D3:9-Pad2): track 7.76 -> 6.17 mm
- net Col16: track 270.6 -> 271.5 mm
- net Row1: track 388.5 -> 389.1 mm, vias 0 -> 2
- net +5V: track 358.7 -> 358.0 mm
- net Net-(J1-Pad2): track 91.4 -> 90.8 mm
- net Net-(J1-Pad3): track 91.5 -> 90.8 mm
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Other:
- board text added: "NeXT76 by Andrew D Rev 1.2"
- board text removed: "NeXT76 by Andrew D Rev 1.1"

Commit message: Extend USB port mount
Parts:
- moved R7 11.0 mm to (370.7, 96.5), turned to -90 degrees
- moved R6 10.8 mm to (133.8, 88.8)
- moved LED3 2.54 mm to (370.7, 91.0), turned to 0 degrees
- moved LED2 2.54 mm to (137.2, 91.0), turned to 0 degrees
- moved J1 0.82 mm to (204.8, 27.8)
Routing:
- net GND: track 515.9 -> 487.4 mm, vias 7 -> 6
- net Row3: track 397.7 -> 389.7 mm
- net Net-(LED2-Pad2): track 89.2 -> 85.6 mm
- net Net-(LED3-Pad2): track 188.3 -> 189.9 mm, vias 1 -> 0
- net Net-(LED2-Pad1): track 5.29 -> 4.01 mm
- net Net-(J1-Pad2): track 90.8 -> 91.7 mm
- net Net-(J1-Pad3): track 90.8 -> 91.7 mm
- net +5V: track 358.0 -> 358.9 mm
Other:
- board size 351.4 x 99.7 mm -> 351.4 x 100.4 mm
